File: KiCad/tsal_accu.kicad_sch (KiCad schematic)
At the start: 41 parts, among them Q5 SQ2308CES, Q6 SQ2308CES, Q7 BSS84AK, Q8 BSS84AK, U1 SN74HCS08, U27 SN74HCS08, U29 SN74LVC74AQPW, U30 74HCT08PW, U37 74AHC02PW, U38 SN74HCS7266QPWR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

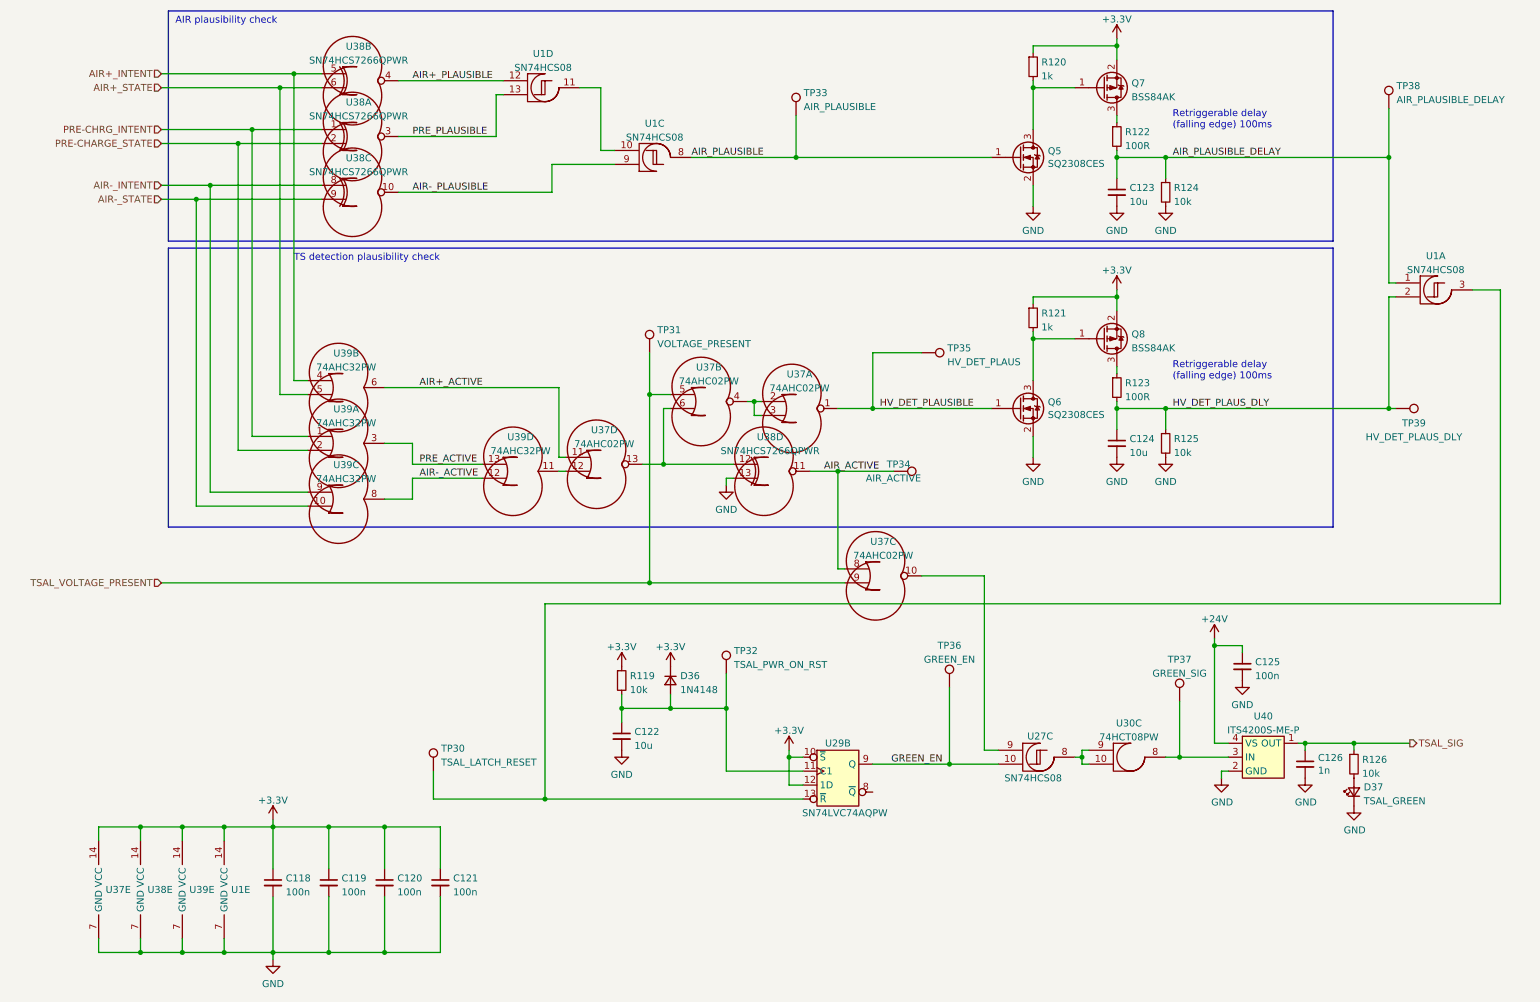
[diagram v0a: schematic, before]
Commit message: Port to Kicad 7, small changes in auto-reset feature
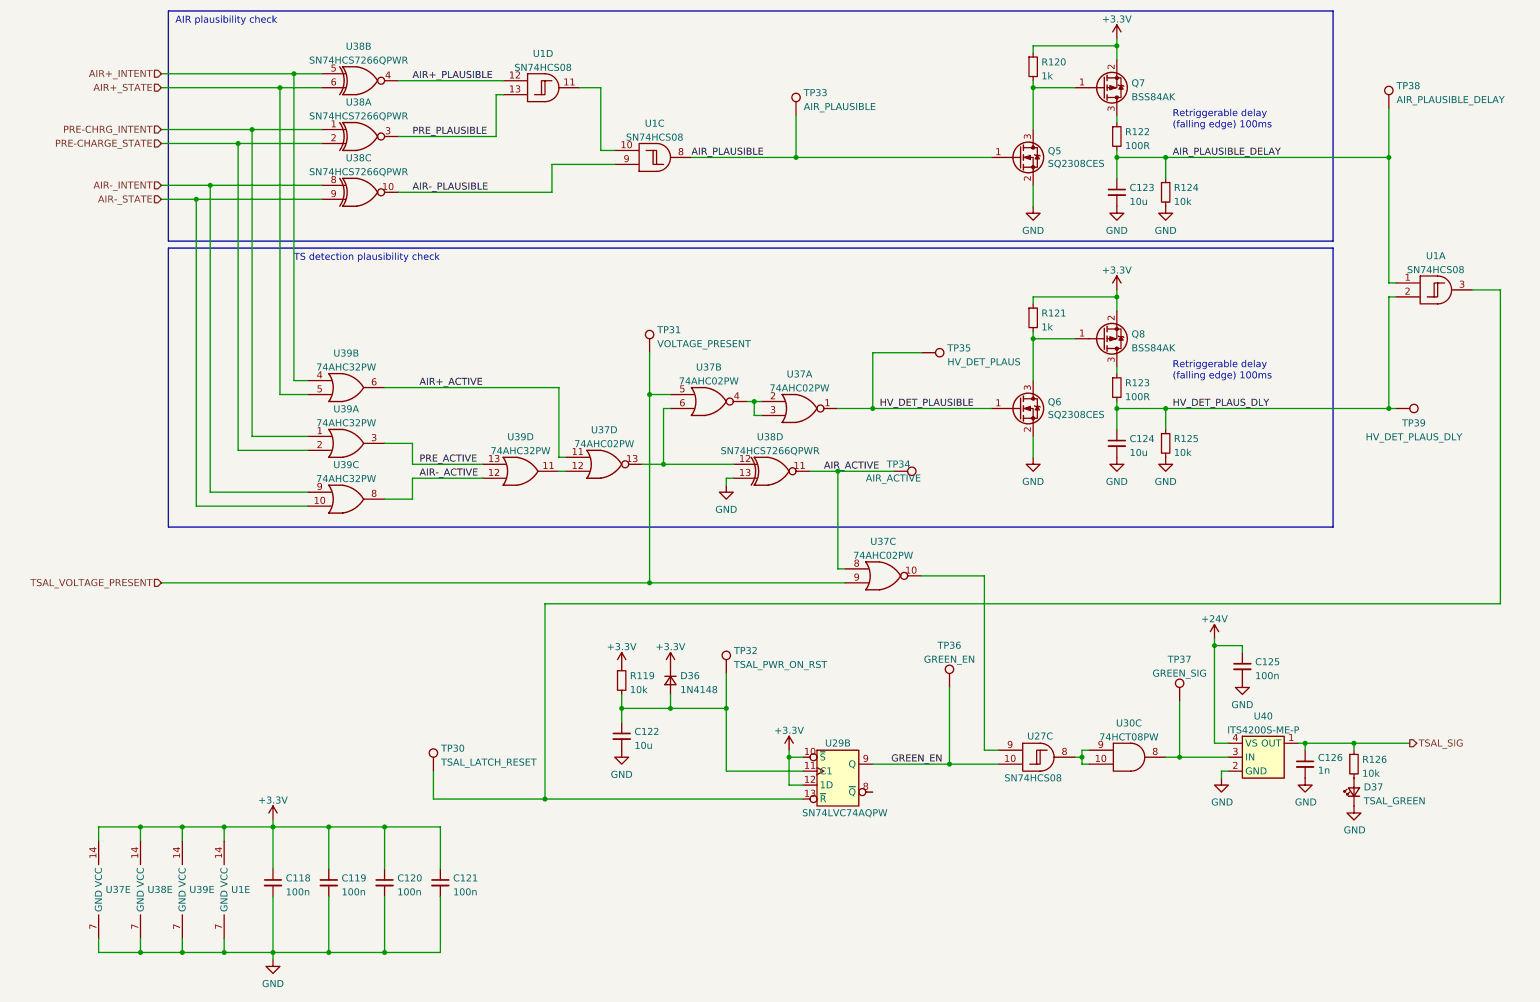
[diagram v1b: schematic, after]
